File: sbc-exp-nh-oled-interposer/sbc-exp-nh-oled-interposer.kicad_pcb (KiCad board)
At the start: 2 copper layers, 52.1 x 10.2 mm, 2 parts, among them J1 P, J2 NH OLED

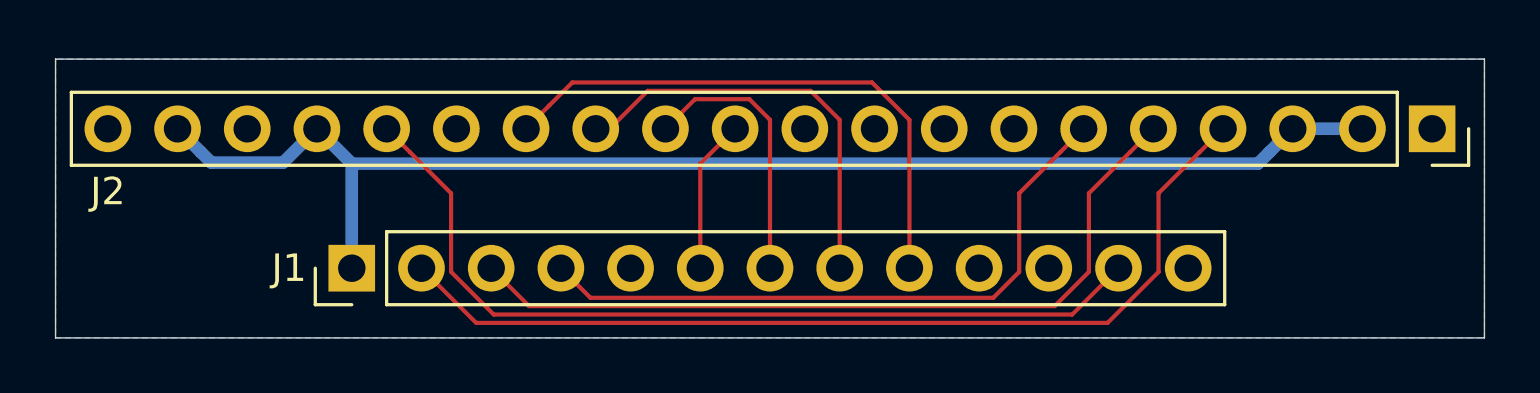
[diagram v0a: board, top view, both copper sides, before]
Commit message: SBC v2.0
Changes:

 - Second VIA
 - NMI button (hardware debounced)
 - 5 status LEDs (power and each VIA port)
 - Ground and power planes
 - Smaller footprint RAM and oscillator
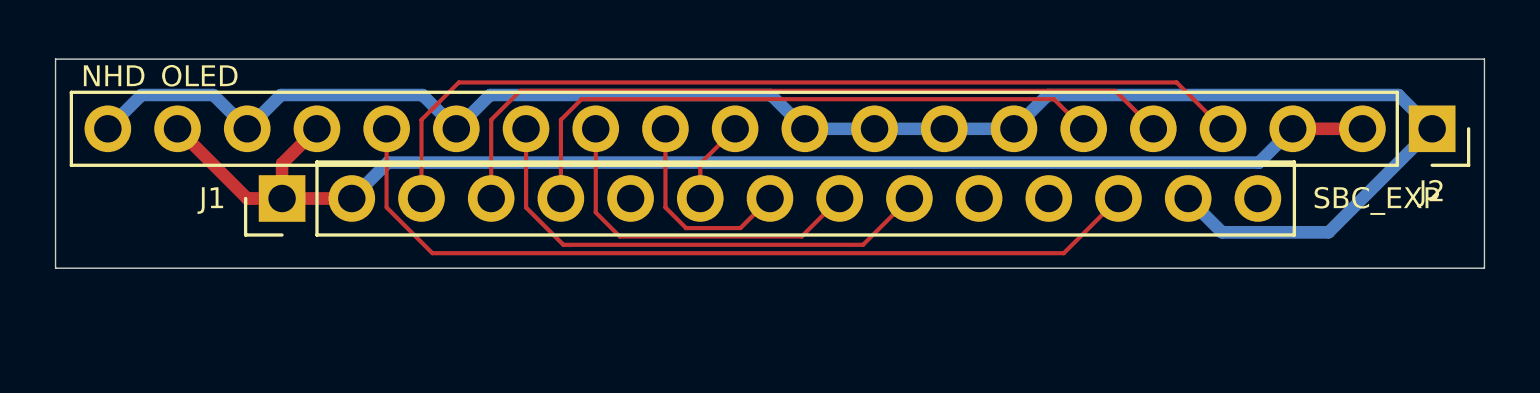
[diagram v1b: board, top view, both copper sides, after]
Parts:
- J1: value P -> SBC_EXP; footprint pin_header:PinHeader_1x13_P2.54mm_Vertical -> pin_header:PinHeader_1x15_P2.54mm_Vertical
- J2: value NH OLED -> NHD_OLED
- moved J1 3.59 mm to (124.5, 99.1)
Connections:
- J1 pad 13: GND -> Net-(J1-Pad13)
- J1 pad 2: Net-(J1-Pad2) -> +5V
- J2 pad 11: Net-(J1-Pad6) -> Net-(J1-Pad7)
- J2 pad 12: Net-(J1-Pad7) -> Net-(J1-Pad8)
- J2 pad 13: Net-(J1-Pad8) -> Net-(J1-Pad9)
- J2 pad 14: Net-(J1-Pad9) -> Net-(J1-Pad10)
- J2 pad 16: Net-(J1-Pad12) -> Net-(J1-Pad13)
- J2 pad 4: Net-(J1-Pad2) -> Net-(J1-Pad3)
- J2 pad 5: Net-(J1-Pad3) -> Net-(J1-Pad4)
- J2 pad 6: Net-(J1-Pad4) -> Net-(J1-Pad5)
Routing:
- net GND: track 0.00 -> 63.3 mm
- net Net-(J1-Pad2): track 34.6 -> 0.00 mm
- net Net-(J1-Pad12): track 31.9 -> 0.00 mm
- net Net-(J1-Pad13): track 0.00 -> 31.1 mm
- net Net-(J1-Pad5): track 0.00 -> 22.7 mm
- net Net-(J1-Pad10): track 0.00 -> 18.1 mm
- net Net-(J1-Pad8): track 15.3 -> 7.43 mm
- net Net-(J1-Pad9): track 20.6 -> 12.9 mm
- net Net-(J1-Pad7): track 9.97 -> 3.07 mm
- net Net-(J1-Pad6): track 5.61 -> 0.00 mm
- net Net-(J1-Pad4): track 23.7 -> 28.0 mm
- net Net-(J1-Pad3): track 29.1 -> 33.3 mm
- net +5V: track 49.1 -> 48.4 mm
- removed copper zone on B.Cu, net GND
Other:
- board size 52.1 x 10.2 mm -> 52.1 x 7.6 mm
- board text added: "v2.0 | © 2021 Daniel Picken | https://github.com/dpicken/6502-hw"
- board text removed: "v1.0 | © 2021 Daniel Picken | https://github.com/dpicken/6502-hw"

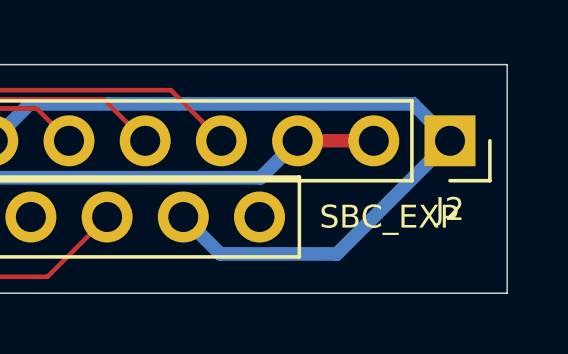
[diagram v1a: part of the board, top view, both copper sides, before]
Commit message: SBC v2.1
Address some v2.0 errata:

  - SBC: Fix LED array layout
  - OLED interposer: Tidy silkscreen
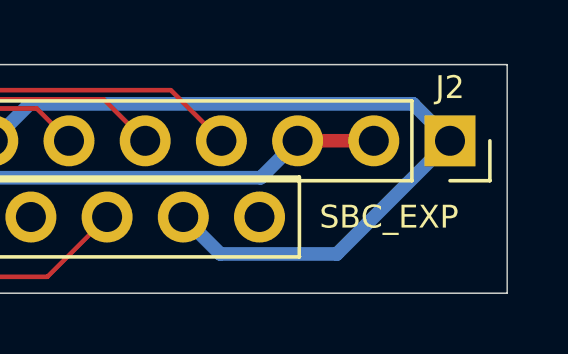
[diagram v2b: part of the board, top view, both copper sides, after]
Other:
- board text added: "v2.1 | © 2021 Daniel Picken | https://github.com/dpicken/6502-hw"
- board text removed: "v2.0 | © 2021 Daniel Picken | https://github.com/dpicken/6502-hw"
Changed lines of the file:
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@@
-(kicad_pcb (version 20171130) (host pcbnew "(5.1.10-1-10_14)")
+(kicad_pcb (version 20171130) (host pcbnew "(5.1.12-1-10_14)")
   (general
     (thickness 1.6002)
@@
   (title_block
     (title "6502 SBC Expansion - NHD 0420CW OLED Interposer")
-    (date 2021-11-10)
-    (rev 2.0)
+    (date 2022-01-13)
+    (rev 2.1)
   )
   (layers
@@
     (descr "Through hole straight socket strip, 1x20, 2.54mm pitch, single row (from Kicad 4.0.7), script generated")
     (tags "Through hole socket strip THT 1x20 2.54mm single row")
-    (fp_text reference J2 (at 2.286 0 180) (layer F.SilkS)
+    (fp_text reference J2 (at -1.778 0 180) (layer F.SilkS)
       (effects (font (size 0.762 0.762) (thickness 0.127)))
     )
@@
       (effects (font (size 0.762 0.762) (thickness 0.127)))
     )
+    (fp_line (start -1.27 -1.27) (end 0.635 -1.27) (layer F.Fab) (width 0.15))
+    (fp_line (start 0.635 -1.27) (end 1.27 -0.635) (layer F.Fab) (width 0.15))
+    (fp_line (start 1.27 -0.635) (end 1.27 49.53) (layer F.Fab) (width 0.15))
+    (fp_line (start 1.27 49.53) (end -1.27 49.53) (layer F.Fab) (width 0.15))
+    (fp_line (start -1.27 49.53) (end -1.27 -1.27) (layer F.Fab) (width 0.15))
+    (fp_line (start -1.33 1.27) (end 1.33 1.27) (layer F.SilkS) (width 0.12))
+    (fp_line (start -1.33 1.27) (end -1.33 49.59) (layer F.SilkS) (width 0.12))
+    (fp_line (start -1.33 49.59) (end 1.33 49.59) (layer F.SilkS) (width 0.12))
+    (fp_line (start 1.33 1.27) (end 1.33 49.59) (layer F.SilkS) (width 0.12))
+    (fp_line (start 1.33 -1.33) (end 1.33 0) (layer F.SilkS) (width 0.12))
+    (fp_line (start 0 -1.33) (end 1.33 -1.33) (layer F.SilkS) (width 0.12))
+    (fp_line (start -1.8 -1.8) (end 1.75 -1.8) (layer F.CrtYd) (width 0.05))
+    (fp_line (start 1.75 -1.8) (end 1.75 50) (layer F.CrtYd) (width 0.05))
+    (fp_line (start 1.75 50) (end -1.8 50) (layer F.CrtYd) (width 0.05))
+    (fp_line (start -1.8 50) (end -1.8 -1.8) (layer F.CrtYd) (width 0.05))
     (fp_text user %R (at 0 24.13) (layer F.Fab)
       (effects (font (size 0.762 0.762) (thickness 0.127)))
     )
-    (fp_line (start -1.8 50) (end -1.8 -1.8) (layer F.CrtYd) (width 0.05))
-    (fp_line (start 1.75 50) (end -1.8 50) (layer F.CrtYd) (width 0.05))
-    (fp_line (start 1.75 -1.8) (end 1.75 50) (layer F.CrtYd) (width 0.05))
-    (fp_line (start -1.8 -1.8) (end 1.75 -1.8) (layer F.CrtYd) (width 0.05))
-    (fp_line (start 0 -1.33) (end 1.33 -1.33) (layer F.SilkS) (width 0.12))
-    (fp_line (start 1.33 -1.33) (end 1.33 0) (layer F.SilkS) (width 0.12))
-    (fp_line (start 1.33 1.27) (end 1.33 49.59) (layer F.SilkS) (width 0.12))
-    (fp_line (start -1.33 49.59) (end 1.33 49.59) (layer F.SilkS) (width 0.12))
-    (fp_line (start -1.33 1.27) (end -1.33 49.59) (layer F.SilkS) (width 0.12))
-    (fp_line (start -1.33 1.27) (end 1.33 1.27) (layer F.SilkS) (width 0.12))
-    (fp_line (start -1.27 49.53) (end -1.27 -1.27) (layer F.Fab) (width 0.15))
-    (fp_line (start 1.27 49.53) (end -1.27 49.53) (layer F.Fab) (width 0.15))
-    (fp_line (start 1.27 -0.635) (end 1.27 49.53) (layer F.Fab) (width 0.15))
-    (fp_line (start 0.635 -1.27) (end 1.27 -0.635) (layer F.Fab) (width 0.15))
-    (fp_line (start -1.27 -1.27) (end 0.635 -1.27) (layer F.Fab) (width 0.15))
     (pad 20 thru_hole oval (at 0 48.26 270) (size 1.7 1.7) (drill 1) (layers *.Cu *.Mask)
       (net 12 GND))
@@
       (effects (font (size 0.762 0.762) (thickness 0.127)))
     )
+    (fp_line (start 1.8 -1.8) (end -1.8 -1.8) (layer F.CrtYd) (width 0.05))
+    (fp_line (start 1.8 37.35) (end 1.8 -1.8) (layer F.CrtYd) (width 0.05))
+    (fp_line (start -1.8 37.35) (end 1.8 37.35) (layer F.CrtYd) (width 0.05))
+    (fp_line (start -1.8 -1.8) (end -1.8 37.35) (layer F.CrtYd) (width 0.05))
+    (fp_line (start -1.33 -1.33) (end 0 -1.33) (layer F.SilkS) (width 0.12))
+    (fp_line (start -1.33 0) (end -1.33 -1.33) (layer F.SilkS) (width 0.12))
+    (fp_line (start -1.33 1.27) (end 1.33 1.27) (layer F.SilkS) (width 0.12))
+    (fp_line (start 1.33 1.27) (end 1.33 36.89) (layer F.SilkS) (width 0.12))
+    (fp_line (start -1.33 1.27) (end -1.33 36.89) (layer F.SilkS) (width 0.12))
+    (fp_line (start -1.33 36.89) (end 1.33 36.89) (layer F.SilkS) (width 0.12))
+    (fp_line (start -1.27 -0.635) (end -0.635 -1.27) (layer F.Fab) (width 0.15))
+    (fp_line (start -1.27 36.83) (end -1.27 -0.635) (layer F.Fab) (width 0.15))
+    (fp_line (start 1.27 36.83) (end -1.27 36.83) (layer F.Fab) (width 0.15))
+    (fp_line (start 1.27 -1.27) (end 1.27 36.83) (layer F.Fab) (width 0.15))
     (fp_line (start -0.635 -1.27) (end 1.27 -1.27) (layer F.Fab) (width 0.15))
-    (fp_line (start 1.27 -1.27) (end 1.27 36.83) (layer F.Fab) (width 0.15))
-    (fp_line (start 1.27 36.83) (end -1.27 36.83) (layer F.Fab) (width 0.15))
-    (fp_line (start -1.27 36.83) (end -1.27 -0.635) (layer F.Fab) (width 0.15))
-    (fp_line (start -1.27 -0.635) (end -0.635 -1.27) (layer F.Fab) (width 0.15))
-    (fp_line (start -1.33 36.89) (end 1.33 36.89) (layer F.SilkS) (width 0.12))
-    (fp_line (start -1.33 1.27) (end -1.33 36.89) (layer F.SilkS) (width 0.12))
-    (fp_line (start 1.33 1.27) (end 1.33 36.89) (layer F.SilkS) (width 0.12))
-    (fp_line (start -1.33 1.27) (end 1.33 1.27) (layer F.SilkS) (width 0.12))
-    (fp_line (start -1.33 0) (end -1.33 -1.33) (layer F.SilkS) (width 0.12))
-    (fp_line (start -1.33 -1.33) (end 0 -1.33) (layer F.SilkS) (width 0.12))
-    (fp_line (start -1.8 -1.8) (end -1.8 37.35) (layer F.CrtYd) (width 0.05))
-    (fp_line (start -1.8 37.35) (end 1.8 37.35) (layer F.CrtYd) (width 0.05))
-    (fp_line (start 1.8 37.35) (end 1.8 -1.8) (layer F.CrtYd) (width 0.05))
-    (fp_line (start 1.8 -1.8) (end -1.8 -1.8) (layer F.CrtYd) (width 0.05))
     (fp_text user %R (at 0 17.78) (layer F.Fab)
       (effects (font (size 0.762 0.762) (thickness 0.127)))
@@
   (gr_line (start 168.275 101.6) (end 116.205 101.6) (layer Edge.Cuts) (width 0.05))
   (gr_line (start 168.275 93.98) (end 168.275 101.6) (layer Edge.Cuts) (width 0.05))
-  (gr_text "v2.0 | © 2021 Daniel Picken | https://github.com/dpicken/6502-hw" (at 163.234072 100.838) (layer B.SilkS)
+  (gr_text "v2.1 | © 2021 Daniel Picken | https://github.com/dpicken/6502-hw" (at 163.234072 100.838) (layer B.SilkS)
     (effects (font (size 0.762 0.762) (thickness 0.127)) (justify left mirror))
   )
